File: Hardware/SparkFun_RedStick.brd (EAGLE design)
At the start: 17.8 x 66 mm, 38 parts, among them Q1 DMG2307L, U2 ATMEGA328P_TQFP, U3 CY7C65213, U4 NCP1402, Y1 16MHZ

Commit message: ready for peer review
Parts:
- moved FRAME2 35.9 mm to (-20.1, -29.3)
- moved L1 0.51 mm to (3.83, 41.0)
- moved LOGO1 0.28 mm to (5.74, 52.5)
- moved U4 0.25 mm to (7.95, 35.7)
- moved D4 0.25 mm to (3.42, 35.3)
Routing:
- net GND: track 30.0 -> 25.2 mm, vias 18 -> 24
- net VBAT: track 15.4 -> 14.8 mm
- net N$8: track 9.20 -> 9.71 mm
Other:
- board text added: "+"
- board text added: "-"
- board text added: "2-5V"
- board text added: "G"
- board text added: "PCB Thickness: 0.078 inch"
- board text added: "PWR"
- board text added: "v01"
- board text removed: "0.13"
- board text removed: "5V"
- board text removed: "DTR"

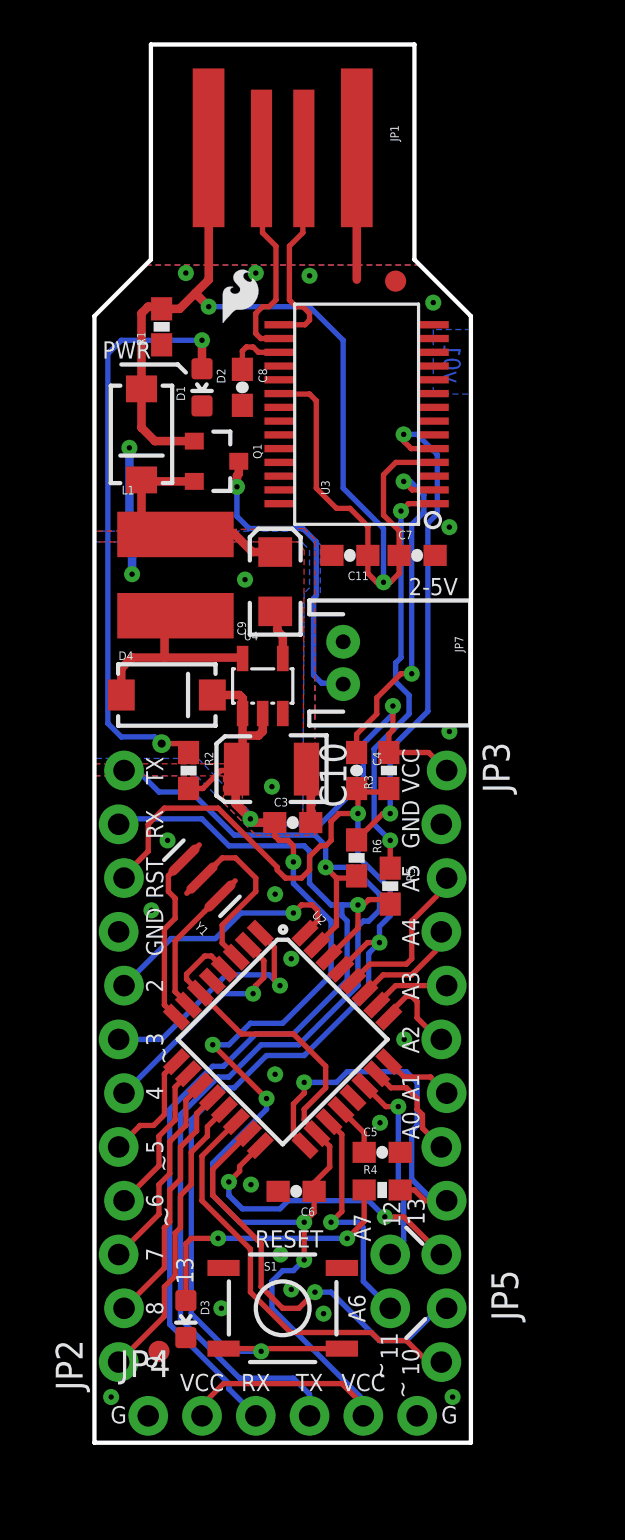
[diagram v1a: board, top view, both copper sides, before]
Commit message: New FTDI and serial pinout
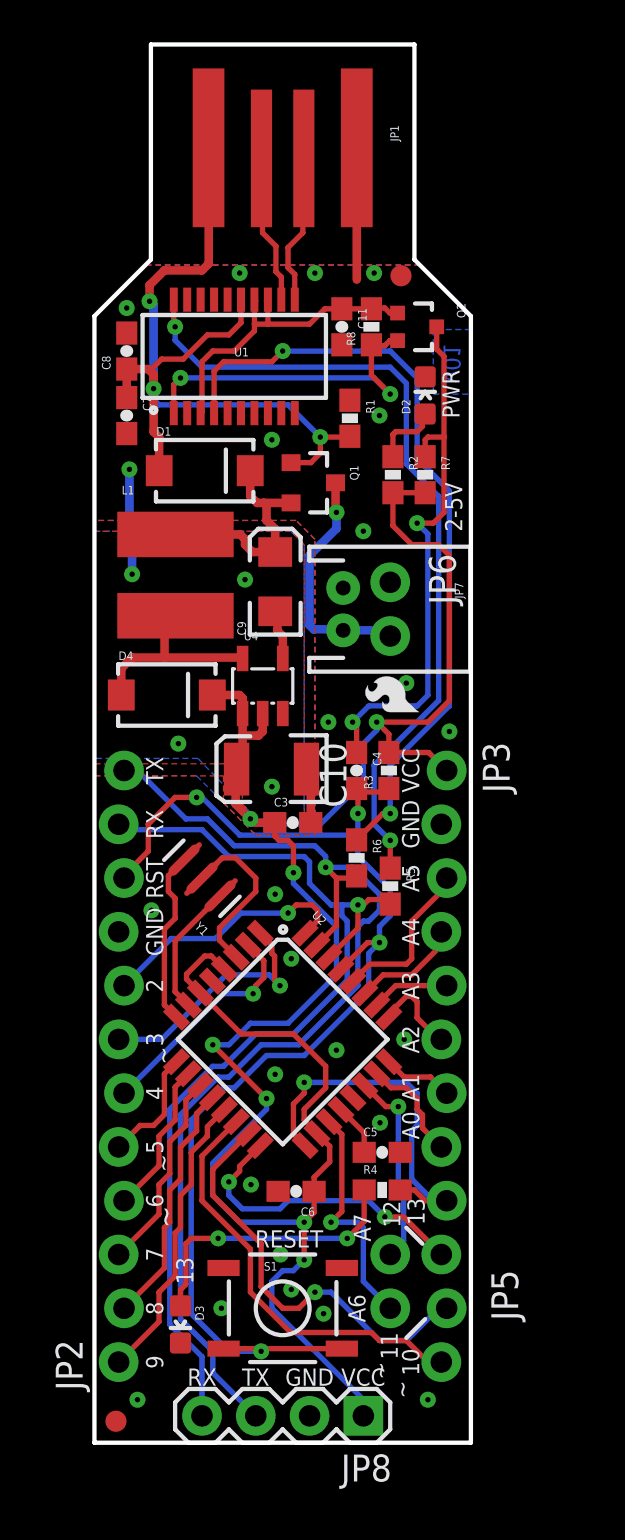
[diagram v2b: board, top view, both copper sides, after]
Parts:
- removed JP4: (no value), SparkFun-Connectors:1X06_NO_SILK_YES_STOP
- removed U3: CY7C65213, SparkFun-DigitalIC:SSOP28DB
- added JP6: M021X02_NO_SILK, SparkFun-Connectors:1X02_NO_SILK
- added JP8: (no value), SparkFun-Connectors:1X04
- added Q2: MOSFET-NCHANNEL2N7002PW, SparkFun-DiscreteSemi:SOT323
- added R7, R8: 10K, SparkFun-Resistors:0603-RES
- added U1: FTS31XS-U, SparkFun-DigitalIC:SSOP20_L
- moved LOGO1 20.9 mm to (15.7, 34.2), turned to 90 degrees
- moved R2 17.0 mm to (14.1, 45.7)
- moved C7 15.2 mm to (1.52, 48.5), turned to 270 degrees
- moved C11 10.8 mm to (11.7, 52.7), turned to 270 degrees
- moved D2 10.5 mm to (15.6, 49.5), turned to 0 degrees
- moved R1 9.88 mm to (12.1, 48.4), turned to 270 degrees
- moved C8 5.72 mm to (1.52, 51.6), turned to 90 degrees
- moved Q1 4.68 mm to (10.3, 45.3)
- moved FID1 3.88 mm to (1.02, 1.02)
- moved U$1 3.81 mm to (14.7, 44.0)
- moved D1 3.44 mm to (5.21, 45.9), turned to 0 degrees
- moved LOGO2 2.62 mm to (4.64, 38.4)
- moved JP7 2.54 mm to (11.7, 39.4)
- moved FID2 0.36 mm to (14.5, 55.1)
- moved D3 0.36 mm to (4.06, 5.59)
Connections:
- removed net N$2: C8.1, U3.17
- new net 3.3V: C11.1, Q2.1, R8.2, U1.13, U1.14, U1.3
- new net N$11: Q2.2, R8.1, U1.1
- net D+: now also U1.11; no longer U3.15
- net D-: now also U1.12; no longer U3.16
- net DTR: now also Q2.3, R7.1; no longer U3.2
- net GND: now also JP6.1, JP8.2, U1.16, U1.6; no longer JP4.1, JP4.6, U3.11, U3.18, U3.21, U3.25, U3.26, U3.7
- net N$3: now also U1.20; no longer U3.1
- net N$7: now also U1.4; no longer U3.5
- net RXI: now also JP8.4; no longer JP4.3
- net TXO: now also JP8.3; no longer JP4.4
- net VBAT: now also JP6.2
- net VCC: now also JP8.1, R7.2; no longer JP4.2, JP4.5
- net V_USB: now also C8.1, U1.15; no longer C11.1, U3.20, U3.4
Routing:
- net N$4: track 27.9 -> 3.25 mm, vias 2 -> 0
- net V_USB: track 59.3 -> 40.3 mm, vias 2 -> 3
- net N$3: track 19.9 -> 38.8 mm
- net N$11: track 0.00 -> 16.1 mm, vias 0 -> 2
- net 3.3V: track 0.00 -> 15.5 mm
- net N$7: track 23.9 -> 37.0 mm
- net DTR: track 16.6 -> 26.1 mm
- net VCC: track 99.8 -> 103.5 mm
- net VBAT: track 14.8 -> 11.3 mm
- net D-: track 10.3 -> 7.06 mm
- net D+: track 10.0 -> 7.11 mm
- net TXO: track 54.4 -> 51.5 mm
- net N$2: track 2.79 -> 0.00 mm
- net RESET: track 61.3 -> 58.6 mm, vias 3 -> 4
- net RXI: track 50.0 -> 48.4 mm
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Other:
- board text removed: "G"

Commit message: ready for review
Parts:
- C10: device SparkFun:EIA3528 -> SparkFun-Capacitors:EIA3528
- C9: device SparkFun:EIA3216 -> SparkFun-Capacitors:EIA3216
- D4: device SparkFun:SMA-DIODE -> SparkFun-DiscreteSemi:SMA-DIODE
- JP1: value USBPCB -> USBPCB_NOPASTE; device SparkFun-Connectors:USB-A-PCB -> SparkFun-Connectors:USB-A-PCB-NOPASTE
- JP2, JP3, JP7, JP8: value (none) -> DNP
- L1: device SparkFun:CR54 -> SparkFun-Passives:CR54
- U4: value NCP1402 -> 5.0v; device SparkFun:SOT23-5 -> SparkFun-PowerIC:SOT23-5
- moved LOGO1 0.57 mm to (15.9, 33.7)
- moved JP6 0.38 mm to (13.6, 40.6)
- moved Q2 0.36 mm to (15.5, 52.5)
- moved C11 0.25 mm to (11.9, 52.7)
- moved R8 0.25 mm to (13.3, 52.7)
- moved C7 0.13 mm to (1.40, 48.5)
- moved C8 0.13 mm to (1.40, 51.6)
- moved R1 0.13 mm to (11.9, 48.4)
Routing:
- net VCC_1: track 12.8 -> 10.8 mm
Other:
- board text added: "Note on paneling:"
- board text added: "RXI"
- board text added: "Route"
- board text added: "TXO"
- board text added: "V-score"

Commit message: fixed errors
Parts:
- moved LOGO2 24.7 mm to (10.7, 14.4), turned to 90 degrees
- moved U$1 4.25 mm to (10.5, 43.9), turned to 90 degrees
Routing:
- net N$6: track 7.28 -> 8.30 mm
- net N$5: track 5.38 -> 6.39 mm
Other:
- board text added: "Marshall Taylor"
- board text added: "RedStick"
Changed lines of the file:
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@@
 <grid distance="0.01" unitdist="inch" unit="inch" style="dots" multiple="1" display="yes" altdistance="0.005" altunitdist="inch" altunit="inch"/>
 <layers>
-<layer number="1" name="Top" color="4" fill="1" visible="yes" active="yes"/>
-<layer number="2" name="Route2" color="1" fill="3" visible="yes" active="yes"/>
-<layer number="15" name="Route15" color="4" fill="6" visible="yes" active="yes"/>
+<layer number="1" name="Top" color="4" fill="1" visible="no" active="yes"/>
+<layer number="2" name="Route2" color="1" fill="3" visible="no" active="yes"/>
+<layer number="15" name="Route15" color="4" fill="6" visible="no" active="yes"/>
 <layer number="16" name="Bottom" color="1" fill="1" visible="yes" active="yes"/>
 <layer number="17" name="Pads" color="2" fill="1" visible="yes" active="yes"/>
@@
 <layer number="19" name="Unrouted" color="6" fill="1" visible="yes" active="yes"/>
 <layer number="20" name="Dimension" color="15" fill="1" visible="yes" active="yes"/>
-<layer number="21" name="tPlace" color="16" fill="1" visible="yes" active="yes"/>
+<layer number="21" name="tPlace" color="16" fill="1" visible="no" active="yes"/>
 <layer number="22" name="bPlace" color="14" fill="1" visible="yes" active="yes"/>
-<layer number="23" name="tOrigins" color="15" fill="1" visible="yes" active="yes"/>
+<layer number="23" name="tOrigins" color="15" fill="1" visible="no" active="yes"/>
 <layer number="24" name="bOrigins" color="15" fill="1" visible="yes" active="yes"/>
-<layer number="25" name="tNames" color="7" fill="1" visible="yes" active="yes"/>
-<layer number="26" name="bNames" color="7" fill="1" visible="yes" active="yes"/>
-<layer number="27" name="tValues" color="7" fill="1" visible="yes" active="yes"/>
-<layer number="28" name="bValues" color="7" fill="1" visible="yes" active="yes"/>
-<layer number="29" name="tStop" color="7" fill="3" visible="yes" active="yes"/>
-<layer number="30" name="bStop" color="7" fill="6" visible="yes" active="yes"/>
-<layer number="31" name="tCream" color="7" fill="4" visible="yes" active="yes"/>
-<layer number="32" name="bCream" color="7" fill="5" visible="yes" active="yes"/>
-<layer number="39" name="tKeepout" color="4" fill="11" visible="yes" active="yes"/>
-<layer number="40" name="bKeepout" color="1" fill="11" visible="yes" active="yes"/>
-<layer number="41" name="tRestrict" color="4" fill="10" visible="yes" active="yes"/>
-<layer number="42" name="bRestrict" color="1" fill="10" visible="yes" active="yes"/>
-<layer number="43" name="vRestrict" color="2" fill="10" visible="yes" active="yes"/>
-<layer number="44" name="Drills" color="7" fill="1" visible="yes" active="yes"/>
-<layer number="45" name="Holes" color="7" fill="1" visible="yes" active="yes"/>
-<layer number="46" name="Milling" color="3" fill="1" visible="yes" active="yes"/>
-<layer number="47" name="Measures" color="7" fill="1" visible="yes" active="yes"/>
-<layer number="51" name="tDocu" color="6" fill="1" visible="yes" active="yes"/>
-<layer number="52" name="bDocu" color="7" fill="1" visible="yes" active="yes"/>
+<layer number="25" name="tNames" color="7" fill="1" visible="no" active="yes"/>
+<layer number="26" name="bNames" color="7" fill="1" visible="no" active="yes"/>
+<layer number="27" name="tValues" color="7" fill="1" visible="no" active="yes"/>
+<layer number="28" name="bValues" color="7" fill="1" visible="no" active="yes"/>
+<layer number="29" name="tStop" color="7" fill="3" visible="no" active="yes"/>
+<layer number="30" name="bStop" color="7" fill="6" visible="no" active="yes"/>
+<layer number="31" name="tCream" color="7" fill="4" visible="no" active="yes"/>
+<layer number="32" name="bCream" color="7" fill="5" visible="no" active="yes"/>
+<layer number="39" name="tKeepout" color="4" fill="11" visible="no" active="yes"/>
+<layer number="40" name="bKeepout" color="1" fill="11" visible="no" active="yes"/>
+<layer number="41" name="tRestrict" color="4" fill="10" visible="no" active="yes"/>
+<layer number="42" name="bRestrict" color="1" fill="10" visible="no" active="yes"/>
+<layer number="43" name="vRestrict" color="2" fill="10" visible="no" active="yes"/>
+<layer number="44" name="Drills" color="7" fill="1" visible="no" active="yes"/>
+<layer number="45" name="Holes" color="7" fill="1" visible="no" active="yes"/>
+<layer number="46" name="Milling" color="3" fill="1" visible="no" active="yes"/>
+<layer number="47" name="Measures" color="7" fill="1" visible="no" active="yes"/>
+<layer number="51" name="tDocu" color="6" fill="1" visible="no" active="yes"/>
+<layer number="52" name="bDocu" color="7" fill="1" visible="no" active="yes"/>
 <layer number="3" name="Route3" color="4" fill="3" visible="no" active="no"/>
 <layer number="4" name="Route4" color="1" fill="4" visible="no" active="no"/>
@@
 <layer number="113" name="IDFDebug" color="4" fill="1" visible="no" active="no"/>
 <layer number="114" name="Badge_Outline" color="11" fill="1" visible="no" active="no"/>
-<layer number="115" name="ReferenceISLANDS" color="7" fill="1" visible="yes" active="yes"/>
+<layer number="115" name="ReferenceISLANDS" color="7" fill="1" visible="no" active="yes"/>
 <layer number="116" name="Patch_BOT" color="9" fill="4" visible="no" active="no"/>
 <layer number="118" name="Rect_Pads" color="7" fill="1" visible="no" active="no"/>
@@
 <text x="13.5636" y="36.957" size="1.778" layer="22" font="vector" ratio="15" rot="MR90" align="top-center">+</text>
 <text x="13.5636" y="42.037" size="1.778" layer="22" font="vector" ratio="15" rot="MR90" align="top-center">-</text>
-<text x="9.5504" y="36.83" size="0.8128" layer="22" font="vector" ratio="15" rot="MR90" align="bottom-center">2-5V</text>
+<text x="15.1384" y="39.37" size="0.8128" layer="22" font="vector" ratio="15" rot="MR90" align="bottom-center">2-5V</text>
 <text x="16.891" y="50.038" size="0.8128" layer="16" font="vector" ratio="15" rot="MR270" align="center-right">v01</text>
 <text x="-41.402" y="61.468" size="1.778" layer="51" font="vector" ratio="15" rot="R180" align="center-right">PCB Thickness: 0.078 inch</text>
@@
 <vertex x="-53.086" y="25.908"/>
 </polygon>
+<text x="10.922" y="-29.464" size="1.778" layer="51">Marshall Taylor</text>
+<text x="3.302" y="52.07" size="2.54" layer="22" font="vector" ratio="15" rot="MR270">RedStick</text>
 </plain>
 <attributes>
@@
 </element>
 <element name="LOGO1" library="SparkFun-Aesthetics" package="SFE_LOGO_FLAME_.1" value="SFE_LOGO_FLAME.1_INCH" x="15.9385" y="33.6804" rot="R90"/>
-<element name="LOGO2" library="SparkFun-Aesthetics" package="OSHW-LOGO-S" value="OSHW-LOGOS" x="4.6355" y="38.354" rot="MR0"/>
+<element name="LOGO2" library="SparkFun-Aesthetics" package="OSHW-LOGO-S" value="OSHW-LOGOS" x="10.668" y="14.4145" rot="MR90"/>
 <element name="Q1" library="SparkFun-DiscreteSemi" package="SOT23-3" value="DMG2307L" x="10.287" y="45.339" rot="R270">
 <attribute name="PROD_ID" value="TRANS-11308" x="10.287" y="45.339" size="1.778" layer="27" rot="R270" display="off"/>
@@
 <attribute name="PROD_ID" value="SWCH-08247" x="8.89" y="6.35" size="1.778" layer="27" display="off"/>
 </element>
-<element name="U$1" library="SparkFun-Aesthetics" package="SFE_LOGO_NAME_FLAME_.1" value="SFE_LOGO_NAME_FLAME.1_INCH" x="14.732" y="44.0055" rot="MR0"/>
+<element name="U$1" library="SparkFun-Aesthetics" package="SFE_LOGO_NAME_FLAME_.1" value="SFE_LOGO_NAME_FLAME.1_INCH" x="10.4775" y="43.942" rot="MR90"/>
 <element name="U2" library="SparkFun-DigitalIC" package="TQFP32-08" value="ATMEGA328P_TQFP" x="8.89" y="19.05" rot="R315">
 <attribute name="PROD_ID" value="IC-09069" x="8.89" y="19.05" size="1.778" layer="27" rot="R315" display="off"/>
@@
 <wire x1="3.81" y1="23.70294375" x2="3.81" y2="21.301571875" width="0.254" layer="1"/>
 <wire x1="3.81" y1="21.301571875" x2="4.440459375" y2="20.6711125" width="0.254" layer="1"/>
-<wire x1="5.21010625" y1="25.10305" x2="5.928528125" y2="25.82146875" width="0" layer="19" extent="1-1"/>
+<wire x1="5.21010625" y1="25.10305" x2="5.210109375" y2="25.10305" width="0.254" layer="1"/>
+<wire x1="5.210109375" y1="25.10305" x2="5.928528125" y2="25.82146875" width="0.254" layer="1"/>
 </signal>
 <signal name="N$6">
@@
 <wire x1="3.4925" y1="26.77955625" x2="3.51305" y2="26.80010625" width="0.254" layer="1"/>
 <wire x1="3.302" y1="24.257" x2="3.302" y2="20.678196875" width="0.254" layer="1"/>
-<wire x1="3.51305" y1="26.80010625" x2="4.23146875" y2="27.518528125" width="0" layer="19" extent="1-1"/>
+<wire x1="3.51305" y1="26.80010625" x2="3.51305" y2="26.800109375" width="0.254" layer="1"/>
+<wire x1="3.51305" y1="26.800109375" x2="4.23146875" y2="27.518528125" width="0.254" layer="1"/>
 </signal>
 <signal name="N$3">
@@
 </signal>
 </signals>
+<errors>
+</errors>
 </board>
 </drawing>
